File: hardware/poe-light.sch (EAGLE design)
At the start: 44 parts, among them J1 RJ45-8-SHIELD-PTH, U1 TPS2378

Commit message: rc
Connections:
- net TAP1: now also B2.AC2; no longer B1.AC1
- net TAP2: now also B2.AC1; no longer B1.AC2
- net TAP3: now also B1.AC1; no longer B2.AC1
- net TAP4: now also B1.AC2; no longer B2.AC2
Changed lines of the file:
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@@
 </segment>
 <segment>
-<pinref part="B1" gate="G$1" pin="AC1"/>
-<wire x1="81.28" y1="154.94" x2="73.66" y2="154.94" width="0.1524" layer="91"/>
-<label x="73.66" y="154.94" size="1.778" layer="95"/>
+<pinref part="B2" gate="G$1" pin="AC2"/>
+<wire x1="121.92" y1="154.94" x2="129.54" y2="154.94" width="0.1524" layer="91"/>
+<label x="129.54" y="154.94" size="1.778" layer="95" rot="MR0"/>
 </segment>
 </net>
@@
 </segment>
 <segment>
-<pinref part="B1" gate="G$1" pin="AC2"/>
-<wire x1="91.44" y1="154.94" x2="99.06" y2="154.94" width="0.1524" layer="91"/>
-<label x="99.06" y="154.94" size="1.778" layer="95" rot="MR0"/>
+<pinref part="B2" gate="G$1" pin="AC1"/>
+<wire x1="111.76" y1="154.94" x2="104.14" y2="154.94" width="0.1524" layer="91"/>
+<label x="104.14" y="154.94" size="1.778" layer="95"/>
 </segment>
 </net>
@@
 </segment>
 <segment>
-<pinref part="B2" gate="G$1" pin="AC1"/>
-<wire x1="111.76" y1="154.94" x2="104.14" y2="154.94" width="0.1524" layer="91"/>
-<label x="104.14" y="154.94" size="1.778" layer="95"/>
+<pinref part="B1" gate="G$1" pin="AC1"/>
+<wire x1="81.28" y1="154.94" x2="73.66" y2="154.94" width="0.1524" layer="91"/>
+<label x="73.66" y="154.94" size="1.778" layer="95"/>
 </segment>
 </net>
@@
 </segment>
 <segment>
-<pinref part="B2" gate="G$1" pin="AC2"/>
-<wire x1="121.92" y1="154.94" x2="129.54" y2="154.94" width="0.1524" layer="91"/>
-<label x="129.54" y="154.94" size="1.778" layer="95" rot="MR0"/>
+<pinref part="B1" gate="G$1" pin="AC2"/>
+<wire x1="91.44" y1="154.94" x2="99.06" y2="154.94" width="0.1524" layer="91"/>
+<label x="99.06" y="154.94" size="1.778" layer="95" rot="MR0"/>
 </segment>
 </net>

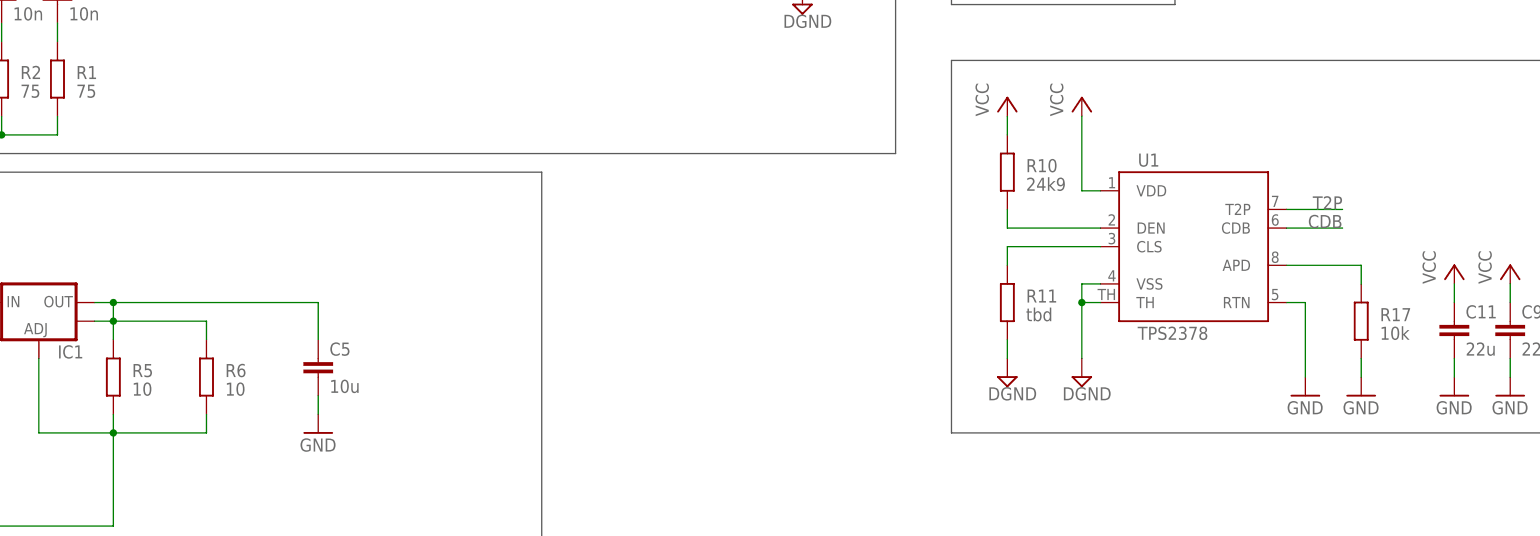
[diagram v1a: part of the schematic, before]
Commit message: hw: adjusted resistor values, added notes about //
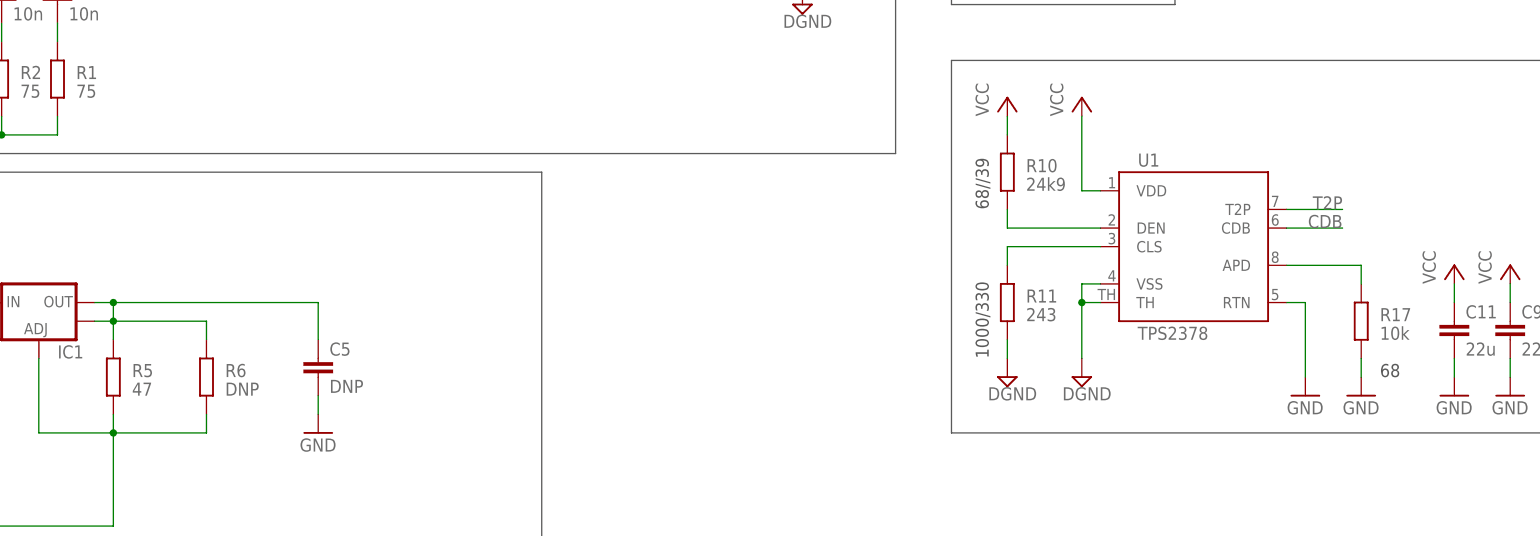
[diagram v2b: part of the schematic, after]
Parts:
- C5: value 10u -> DNP
- R11: value tbd -> 243
- R5: value 10 -> 47
- R6: value 10 -> DNP
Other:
- note added: "1000/330"
- note added: "68"
- note added: "68//39"
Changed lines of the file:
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@@
 <part name="C8" library="rcl" deviceset="C-EU" device="C0603" value=".1u"/>
 <part name="R10" library="rcl" deviceset="R-EU_" device="R0603" value="24k9"/>
-<part name="R11" library="rcl" deviceset="R-EU_" device="R0603" value="tbd"/>
+<part name="R11" library="rcl" deviceset="R-EU_" device="R0603" value="243"/>
 <part name="P+2" library="supply1" deviceset="VCC" device=""/>
 <part name="P+3" library="supply1" deviceset="VCC" device=""/>
@@
 <part name="IC1" library="SparkFun-PowerIC" deviceset="V_REG_LM1117" device="SOT223"/>
 <part name="P+1" library="supply1" deviceset="VCC" device=""/>
-<part name="R5" library="rcl" deviceset="R-EU_" device="R1206" value="10"/>
-<part name="C5" library="rcl" deviceset="C-EU" device="C0805" value="10u"/>
+<part name="R5" library="rcl" deviceset="R-EU_" device="R1206" value="47"/>
+<part name="C5" library="rcl" deviceset="C-EU" device="C0805" value="DNP"/>
 <part name="GND7" library="supply1" deviceset="GND" device=""/>
 <part name="D10" library="balto" deviceset="LED_XH-G" device=""/>
 <part name="GND8" library="supply1" deviceset="GND" device=""/>
-<part name="R6" library="rcl" deviceset="R-EU_" device="R1206" value="10"/>
+<part name="R6" library="rcl" deviceset="R-EU_" device="R1206" value="DNP"/>
 <part name="D2" library="balto" deviceset="LED_XH-G" device=""/>
 <part name="D3" library="balto" deviceset="LED_XH-G" device=""/>
@@
 <wire x1="2.54" y1="2.54" x2="2.54" y2="114.3" width="0.1524" layer="97"/>
 <text x="5.08" y="106.68" size="5.08" layer="97">Main LEDs</text>
+<text x="180.34" y="109.22" size="1.778" layer="97" rot="R90">68//39</text>
+<text x="180.34" y="88.9" size="1.778" layer="97" rot="R90">1000/330</text>
+<text x="233.68" y="86.36" size="1.778" layer="97">68</text>
 </plain>
 <instances>

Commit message: hw: sch: layout clean
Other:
- note added: "Input + rectifier"
- note added: "LEDs"
- note added: "PoE Controller"
- note added: "Power LEDs"
- note removed: "Main LEDs"
- moved on the sheet: B1, B2, BOX1, C1, C11, C2, C3, C4, C5, C7, C8, C9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
